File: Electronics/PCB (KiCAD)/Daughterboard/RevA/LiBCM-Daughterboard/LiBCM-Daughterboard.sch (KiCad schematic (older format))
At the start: 43 parts, among them J1 Conn_01x03, J10 Conn_01x02, J11 Conn_01x05, J2 Conn_01x02, J3 Conn_01x07, J4 Conn_01x07, J5 Conn_01x08, J6 Conn_01x02, J7 Conn_01x08, J8 Conn_01x04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

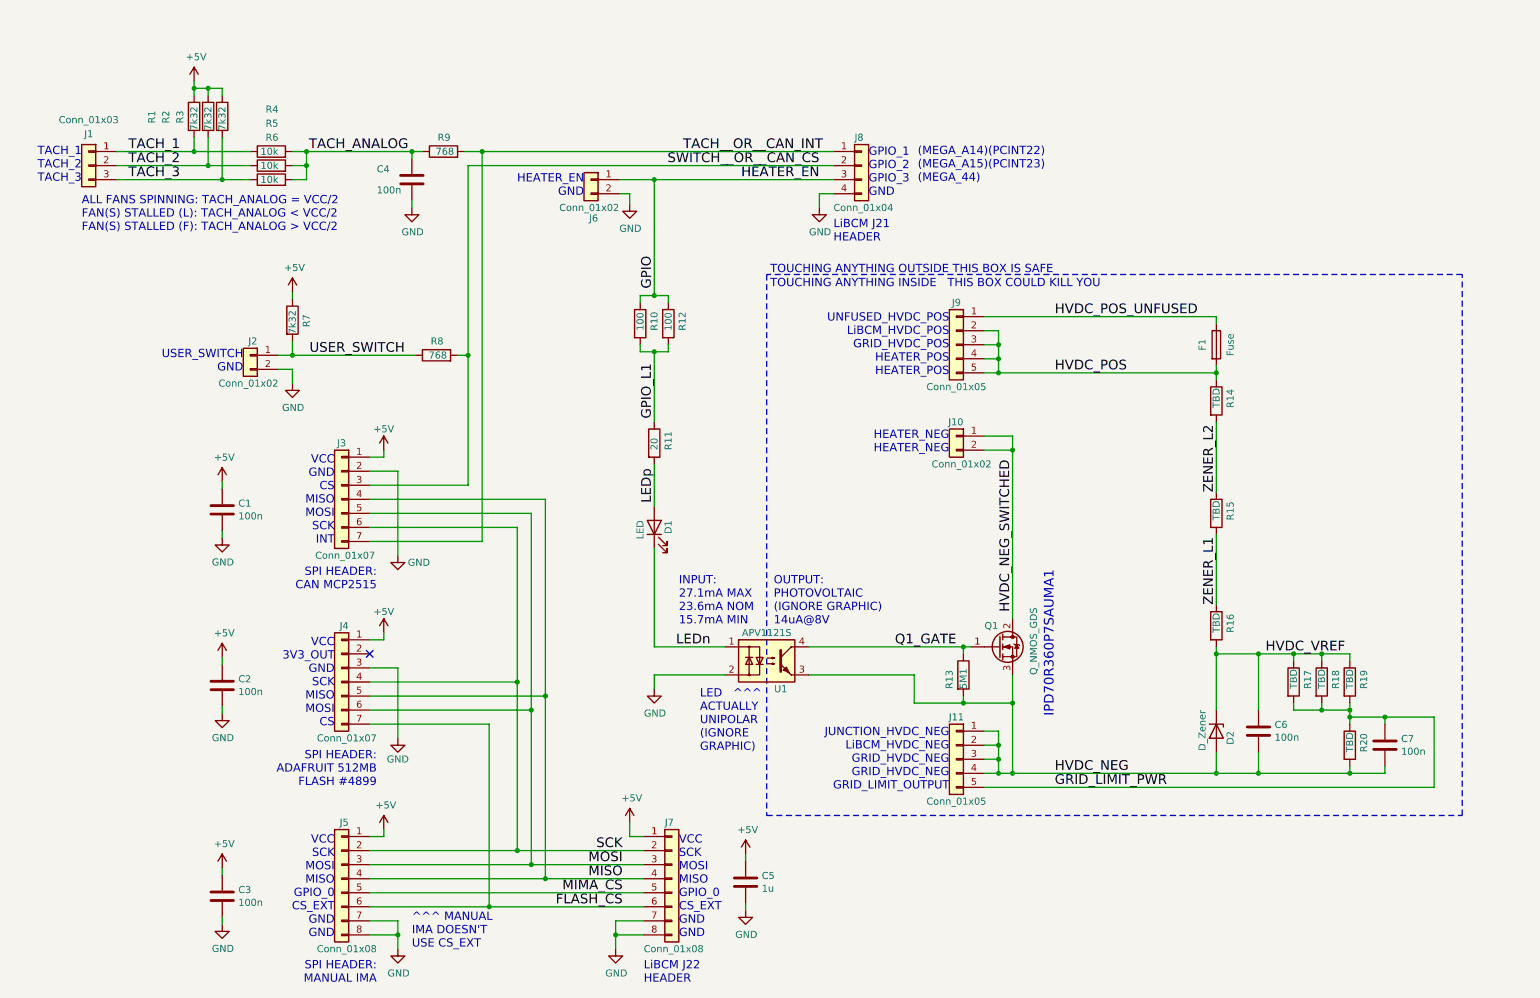
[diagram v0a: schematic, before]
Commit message: RevB Heater PCBs, Daughterboard Schematic
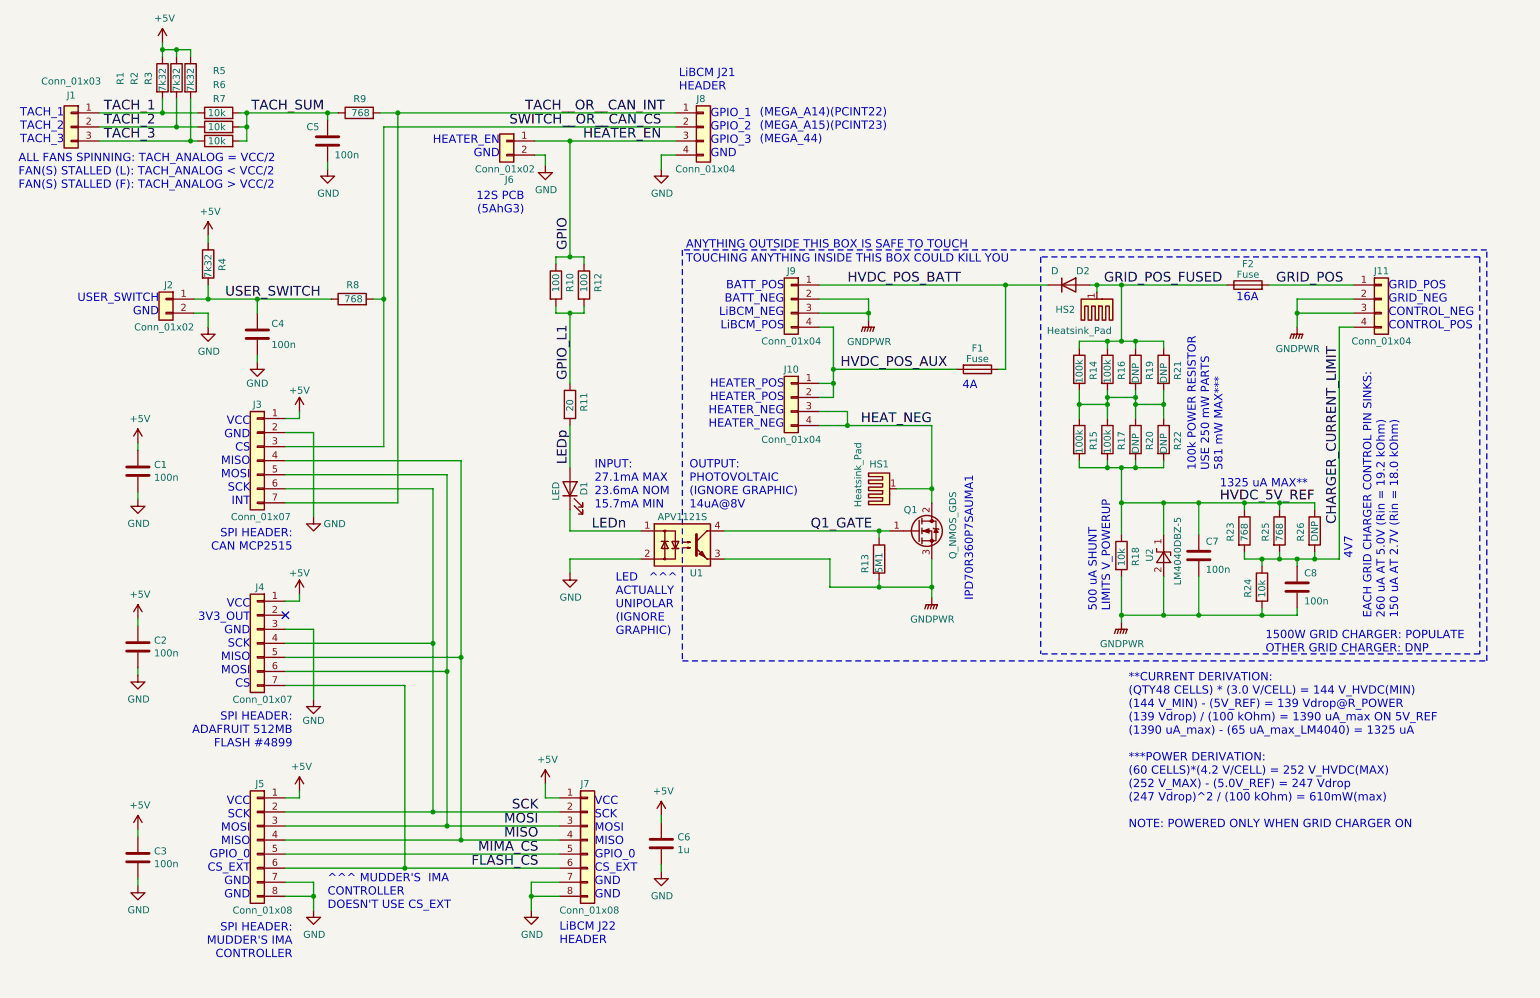
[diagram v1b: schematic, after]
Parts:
- removed D2: D_Zener, symbol Device:D_Zener
- removed J10: Conn_01x02, symbol Connector_Generic:Conn_01x02
- removed J11, J9: Conn_01x05, symbol Connector_Generic:Conn_01x05
- added C4: 100n, Capacitor_SMD:C_0805_2012Metric, symbol Device:C
- added D2: D, symbol Device:D
- added F1: Fuse, Fuse:Fuseholder_Cylinder-5x20mm_Schurter_0031_8201_Horizontal_Open, symbol Device:Fuse
- added HS1, HS2: Heatsink_Pad, symbol Mechanical:Heatsink_Pad
- added J10, J11, J9: Conn_01x04, symbol Connector_Generic:Conn_01x04
- added R17: 100k, Resistor_SMD:R_0805_2012Metric, symbol Device:R
- added R18: 10k, Resistor_SMD:R_0805_2012Metric, symbol Device:R
- added R19, R20, R21, R22: DNP, Resistor_SMD:R_0805_2012Metric, symbol Device:R
- added U2: LM4040DBZ-5, Package_TO_SOT_SMD:SOT-23, symbol Reference_Voltage:LM4040DBZ-5
- C1, C2, C3: footprint (none) -> Capacitor_SMD:C_0805_2012Metric
- C5: renamed from C4; footprint (none) -> Capacitor_SMD:C_0805_2012Metric
- C6: renamed from C5; footprint (none) -> Capacitor_SMD:C_0805_2012Metric
- C7: renamed from C6; footprint (none) -> Capacitor_SMD:C_0805_2012Metric
- C8: renamed from C7; footprint (none) -> Capacitor_SMD:C_0805_2012Metric
- F2: renamed from F1; footprint (none) -> Fuse:Fuseholder_Cylinder-5x20mm_Schurter_0031_8201_Horizontal_Open
- J3, J4: footprint (none) -> Connector_PinHeader_2.54mm:PinHeader_1x07_P2.54mm_Vertical
- J5, J7: footprint (none) -> Connector_PinHeader_2.54mm:PinHeader_1x08_P2.54mm_Horizontal
- J6: footprint (none) -> Connector_PinHeader_2.54mm:PinHeader_1x02_P2.54mm_Horizontal
- J8: footprint (none) -> Connector_PinHeader_2.54mm:PinHeader_1x04_P2.54mm_Vertical
- R1, R10, R11, R12, R2, R3, R8, R9: footprint (none) -> Resistor_SMD:R_0805_2012Metric
- R13: footprint (none) -> Resistor_SMD:R_1206_3216Metric
- R14, R15, R16: value TBD -> 100k; footprint (none) -> Resistor_SMD:R_0805_2012Metric
- R23: renamed from R17; value TBD -> 768; footprint (none) -> Resistor_SMD:R_0805_2012Metric
- R24: renamed from R20; value TBD -> 10k; footprint (none) -> Resistor_SMD:R_0805_2012Metric
- R25: renamed from R18; value TBD -> 768; footprint (none) -> Resistor_SMD:R_0805_2012Metric
- R26: renamed from R19; value TBD -> DNP; footprint (none) -> Resistor_SMD:R_0805_2012Metric
- R4: renamed from R7; footprint (none) -> Resistor_SMD:R_0805_2012Metric
- R5: renamed from R4; footprint (none) -> Resistor_SMD:R_0805_2012Metric
- R6: renamed from R5; footprint (none) -> Resistor_SMD:R_0805_2012Metric
- R7: renamed from R6; footprint (none) -> Resistor_SMD:R_0805_2012Metric
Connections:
- net GND: now also C4.2
- net USER_SWITCH: now also C4.1
- net GRID_LIMIT_PWR renamed CHARGER_CURRENT_LIMIT
- net CHARGER_CURRENT_LIMIT: now also J11.4 (Pin_4)
- net HVDC_NEG renamed GNDPWR
- net GNDPWR: now also J11.2 (Pin_2), J11.3 (Pin_3), J9.2 (Pin_2), J9.3 (Pin_3), R18.2, U2.2 (A)
- net HVDC_NEG_SWITCHED renamed HEAT_NEG
- net HEAT_NEG: now also HS1.1, J10.3 (Pin_3), J10.4 (Pin_4)
- net HVDC_POS renamed GRID_POS
- net GRID_POS: now also J11.1 (Pin_1); no longer R14.1
- net HVDC_POS_UNFUSED renamed GRID_POS_FUSED
- net GRID_POS_FUSED: now also R14.1, R16.1, D2.2 (A), HS2.1, R19.1, R21.1
- net HVDC_VREF renamed HVDC_5V_REF
- net HVDC_5V_REF: now also R15.2, R17.2, R18.1, R20.2, R22.2, U2.1 (K); no longer R16.2
- net TACH_ANALOG renamed TACH_SUM
- removed net ZENER_L1: R15.2, R16.1
- net ZENER_L2: no longer names the net of R14.2, R15.1
- net ZENER_L2: now also R16.2, R17.1, R19.2, R20.1, R21.2, R22.1
- new net HVDC_POS_AUX: F1.2, J10.1 (Pin_1), J10.2 (Pin_2), J9.4 (Pin_4)
- new net HVDC_POS_BATT: D2.1 (K), F1.1, J9.1 (Pin_1)
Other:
- note added: "**CURRENT DERIVATION:\n(QTY48 CELLS) * (3.0 V/CELL) = 144 V_HVDC(MIN)\n(144 V_MIN) - (5V_REF) = 139 Vdrop@R_POWER\n(139 Vdrop) / (100 kOhm) = 1390 uA_max ON 5V_REF\n(1390 uA_max) - (65 uA_max_LM4040) = 1325 uA\n\n***POWER DERIVATION:\n(60 CELLS)*(4.2 V/CELL) = 252 V_HVDC(MAX)\n(252 V_MAX) - (5.0V_REF) = 247 Vdrop\n(247 Vdrop)^2 / (100 kOhm) = 610mW(max)\n\nNOTE: POWERED ONLY WHEN GRID CHARGER ON\n"
- note added: "100k POWER RESISTOR\nUSE 250 mW PARTS\n581 mW MAX***"
- note added: "12S PCB\n(5AhG3)"
- note added: "1325 uA MAX**"
- note added: "1500W GRID CHARGER: POPULATE\nOTHER GRID CHARGER: DNP"
- note added: "16A"
- note added: "4A"
- note added: "4V7"
- note added: "500 uA SHUNT\nLIMITS V_POWERUP"
- note added: "ANYTHING OUTSIDE THIS BOX IS SAFE TO TOUCH"
- note added: "BATT_POS\nBATT_NEG\nLiBCM_NEG\nLiBCM_POS\n"
- note added: "EACH GRID CHARGER CONTROL PIN SINKS:\n260 uA AT 5.0V (Rin = 19.2 kOhm)\n150 uA AT 2.7V (Rin = 18.0 kOhm)\n"
- note added: "GRID_POS\nGRID_NEG\nCONTROL_NEG\nCONTROL_POS"
- note added: "HEATER_POS\nHEATER_POS\nHEATER_NEG\nHEATER_NEG"
- note added: "SPI HEADER:\nMUDDER'S IMA\nCONTROLLER"
- note added: "^^^ MUDDER'S IMA\nCONTROLLER \nDOESN'T USE CS_EXT"
- note removed: "HEATER_NEG\nHEATER_NEG"
- note removed: "JUNCTION_HVDC_NEG\nLiBCM_HVDC_NEG\nGRID_HVDC_NEG\nGRID_HVDC_NEG\nGRID_LIMIT_OUTPUT"
- note removed: "SPI HEADER:\nMANUAL IMA"
- note removed: "TOUCHING ANYTHING OUTSIDE THIS BOX IS SAFE"
- note removed: "UNFUSED_HVDC_POS\nLiBCM_HVDC_POS\nGRID_HVDC_POS\nHEATER_POS\nHEATER_POS"
- note removed: "^^^ MANUAL\nIMA DOESN'T\nUSE CS_EXT"
- moved on the sheet: C1, C2, C3, C5, C6, C7, C8, D1, F2, J1, J2, J3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
